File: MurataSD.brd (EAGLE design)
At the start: 50 x 52 mm, 2 parts, among them U1 IC_BLE_LBCA2HNZYZ-711, U100 BOARD_MMC

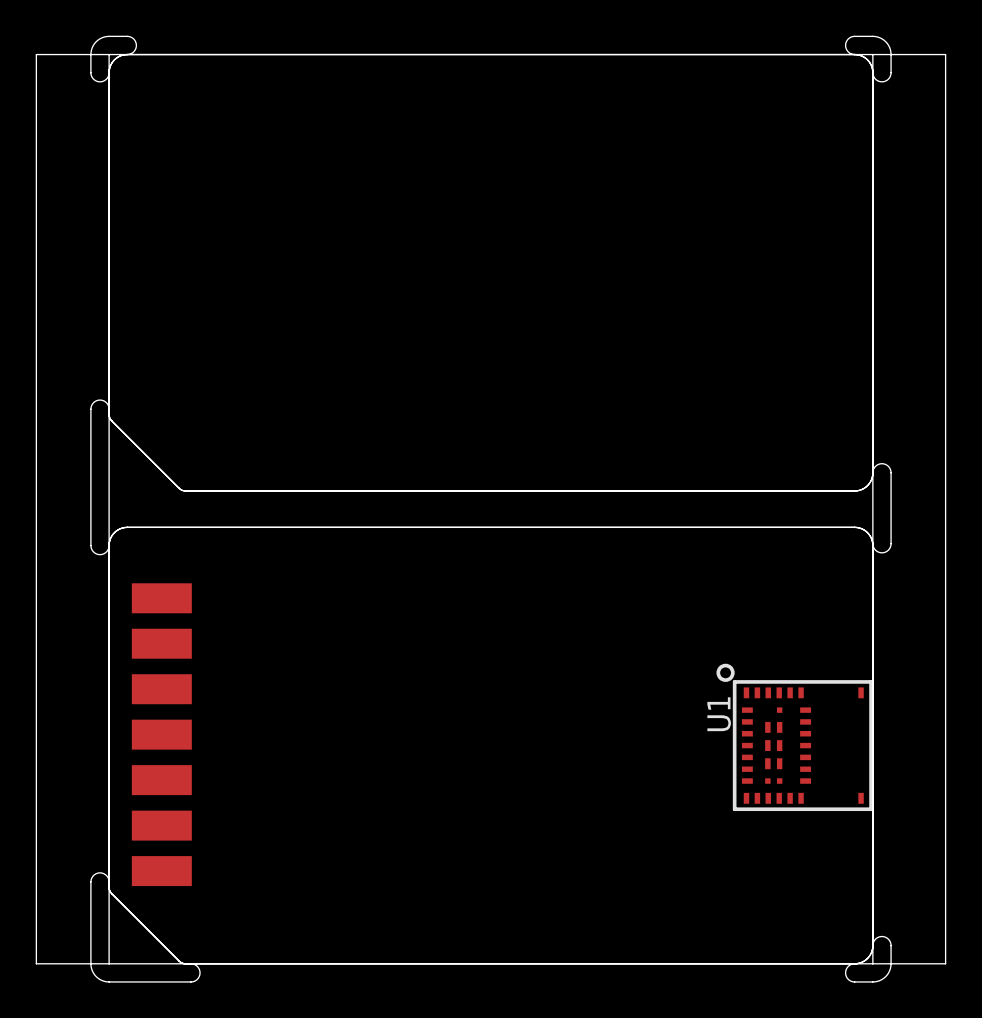
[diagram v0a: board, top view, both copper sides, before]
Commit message: schematic update
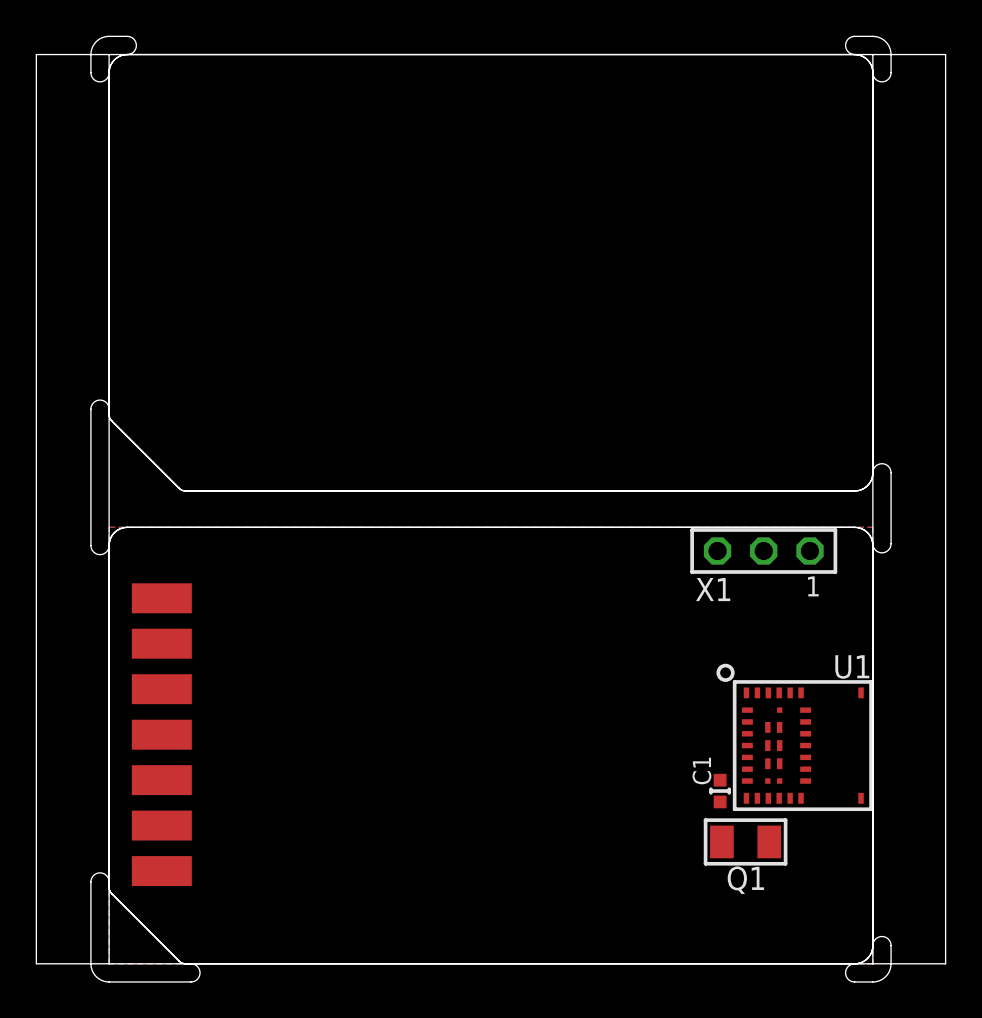
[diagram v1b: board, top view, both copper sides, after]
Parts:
- added C1: (no value), mylib:C0402
- added Q1: (no value), mylib:CR_3216
- added X1: TSW-103-02-S-S, con-samtec.local:TSW-103-02-S-S
- renumbered U100 to U2
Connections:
- new net 3.3V: C1.1, U1.7, U2.4
- new net CLK: U1.23, U2.5
- new net CS: U1.11, U2.1
- new net GND: C1.2, U1.15, U1.16, U1.17, U1.18, U1.20, U1.21, U1.26, U1.27, U1.28, U1.29, U1.32, U1.33, U1.34, U1.6, U1.8, U2.3, U2.6, X1.3
- new net MISO: U1.3, U2.7
- new net MOSI: U1.1, U2.2
- new net N$1: Q1.1, U1.9
- new net N$2: Q1.2, U1.10
- new net N$3: U1.4, X1.1
- new net N$4: U1.5, X1.2
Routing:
- added copper zone on layer 1, net GND
- added copper zone on layer 16, net GND

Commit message: [ SD ] update library
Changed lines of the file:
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@@
 <layers>
 <layer number="1" name="Top" color="4" fill="0" visible="yes" active="yes"/>
+<layer number="2" name="Route2" color="1" fill="3" visible="no" active="no"/>
+<layer number="3" name="Route3" color="4" fill="3" visible="no" active="no"/>
+<layer number="14" name="Route14" color="1" fill="6" visible="no" active="no"/>
+<layer number="15" name="Route15" color="4" fill="6" visible="no" active="no"/>
 <layer number="16" name="Bottom" color="1" fill="1" visible="yes" active="yes"/>
 <layer number="17" name="Pads" color="2" fill="1" visible="yes" active="yes"/>
 <layer number="18" name="Vias" color="2" fill="1" visible="yes" active="yes"/>
 <layer number="19" name="Unrouted" color="6" fill="1" visible="yes" active="yes"/>
-<layer number="20" name="Dimension" color="15" fill="1" visible="no" active="yes"/>
+<layer number="20" name="Dimension" color="15" fill="1" visible="yes" active="yes"/>
 <layer number="21" name="tPlace" color="7" fill="1" visible="yes" active="yes"/>
 <layer number="22" name="bPlace" color="7" fill="1" visible="yes" active="yes"/>
@@
 <layer number="45" name="Holes" color="7" fill="1" visible="no" active="yes"/>
 <layer number="46" name="Milling" color="3" fill="1" visible="no" active="yes"/>
-<layer number="47" name="Measures" color="7" fill="1" visible="no" active="yes"/>
+<layer number="47" name="Measures" color="7" fill="1" visible="yes" active="yes"/>
 <layer number="48" name="Document" color="7" fill="1" visible="yes" active="yes"/>
 <layer number="49" name="Reference" color="7" fill="1" visible="yes" active="yes"/>
@@
 <layer number="132" name="bAdjust" color="7" fill="1" visible="no" active="yes"/>
 <layer number="144" name="Drill_legend" color="7" fill="1" visible="yes" active="yes"/>
+<layer number="145" name="DrillLegend_01-16" color="2" fill="9" visible="no" active="yes"/>
+<layer number="146" name="DrillLegend_01-20" color="3" fill="9" visible="no" active="yes"/>
 <layer number="151" name="HeatSink" color="7" fill="1" visible="yes" active="yes"/>
 <layer number="152" name="_bDocu" color="7" fill="1" visible="yes" active="yes"/>
@@
 </polygon>
 <contactref element="X1" pad="3"/>
-<wire x1="39.05" y1="14.9" x2="37.46" y2="22.7" width="0" layer="19" extent="1-1"/>
-<wire x1="40.225" y1="13" x2="39.05" y2="14.9" width="0" layer="19" extent="1-1"/>
-<wire x1="40.875" y1="13" x2="40.225" y2="13" width="0" layer="19" extent="1-1"/>
-<wire x1="40.875" y1="12" x2="40.875" y2="13" width="0" layer="19" extent="1-1"/>
-<wire x1="40.225" y1="12" x2="40.875" y2="12" width="0" layer="19" extent="1-1"/>
-<wire x1="40.875" y1="11" x2="40.875" y2="12" width="0" layer="19" extent="1-1"/>
-<wire x1="40.225" y1="11" x2="40.875" y2="11" width="0" layer="19" extent="1-1"/>
-<wire x1="39.1" y1="10.7" x2="40.225" y2="11" width="0" layer="19" extent="1-1"/>
-<wire x1="42.3" y1="12" x2="40.875" y2="12" width="0" layer="19" extent="1-1"/>
-<wire x1="42.3" y1="11.35" x2="42.3" y2="12" width="0" layer="19" extent="1-1"/>
-<wire x1="42.3" y1="12.65" x2="42.3" y2="12" width="0" layer="19" extent="1-1"/>
-<wire x1="42.3" y1="10.7" x2="42.3" y2="11.35" width="0" layer="19" extent="1-1"/>
-<wire x1="42.3" y1="13.95" x2="42.3" y2="12.65" width="0" layer="19" extent="1-1"/>
-<wire x1="42.05" y1="14.9" x2="42.3" y2="13.95" width="0" layer="19" extent="1-1"/>
-<wire x1="39.05" y1="9.1" x2="39.1" y2="10.7" width="0" layer="19" extent="1-1"/>
-<wire x1="37.6" y1="8.9" x2="39.05" y2="9.1" width="0" layer="19" extent="1-1"/>
-<wire x1="6.9" y1="10.1" x2="37.6" y2="8.9" width="0" layer="19" extent="1-1"/>
-<wire x1="6.9" y1="17.6" x2="6.9" y2="10.1" width="0" layer="19" extent="1-1"/>
+<wire x1="6.9" y1="10.1" x2="6.9" y2="17.6" width="0" layer="19" extent="1-1"/>
+<wire x1="37.6" y1="8.9" x2="6.9" y2="10.1" width="0" layer="19" extent="1-1"/>
 </signal>
 <signal name="3.3V">
@@
 <contactref element="U1" pad="7"/>
 <contactref element="C1" pad="1"/>
-<wire x1="37.6" y1="10.1" x2="39.1" y2="10.05" width="0" layer="19" extent="1-1"/>
+<wire x1="37.6" y1="10.1" x2="39" y2="10.05" width="0" layer="19" extent="1-1"/>
 <wire x1="6.9" y1="12.6" x2="37.6" y2="10.1" width="0" layer="19" extent="1-1"/>
 </signal>
@@
 <contactref element="U1" pad="9"/>
 <contactref element="Q1" pad="1"/>
-<wire x1="37.7" y1="6.7" x2="39.65" y2="9.1" width="0" layer="19" extent="1-1"/>
+<wire x1="37.7" y1="6.7" x2="39.625" y2="9.1" width="0" layer="19" extent="1-1"/>
 </signal>
 <signal name="N$2">
 <contactref element="U1" pad="10"/>
 <contactref element="Q1" pad="2"/>
-<wire x1="40.3" y1="6.7" x2="40.25" y2="9.1" width="0" layer="19" extent="1-1"/>
+<wire x1="40.3" y1="6.7" x2="40.275" y2="9.1" width="0" layer="19" extent="1-1"/>
 </signal>
 <signal name="CLK">
 <contactref element="U2" pad="5"/>
 <contactref element="U1" pad="23"/>
-<wire x1="6.9" y1="15.1" x2="40.85" y2="14.9" width="0" layer="19" extent="1-1"/>
+<wire x1="6.9" y1="15.1" x2="40.925" y2="14.9" width="0" layer="19" extent="1-1"/>
 </signal>
 <signal name="MOSI">
 <contactref element="U2" pad="2"/>
 <contactref element="U1" pad="1"/>
-<wire x1="6.9" y1="7.6" x2="39.1" y2="13.95" width="0" layer="19" extent="1-1"/>
+<wire x1="6.9" y1="7.6" x2="39" y2="13.95" width="0" layer="19" extent="1-1"/>
 </signal>
 <signal name="CS">
 <contactref element="U2" pad="1"/>
 <contactref element="U1" pad="11"/>
-<wire x1="6.9" y1="5.1" x2="40.85" y2="9.1" width="0" layer="19" extent="1-1"/>
+<wire x1="6.9" y1="5.1" x2="40.925" y2="9.1" width="0" layer="19" extent="1-1"/>
 </signal>
 <signal name="MISO">
 <contactref element="U2" pad="7"/>
 <contactref element="U1" pad="3"/>
-<wire x1="6.9" y1="20.1" x2="39.1" y2="12.65" width="0" layer="19" extent="1-1"/>
+<wire x1="6.9" y1="20.1" x2="39" y2="12.65" width="0" layer="19" extent="1-1"/>
 </signal>
 <signal name="N$3">
 <contactref element="U1" pad="4"/>
 <contactref element="X1" pad="1"/>
-<wire x1="39.1" y1="12" x2="42.54" y2="22.7" width="0" layer="19" extent="1-1"/>
+<wire x1="39" y1="12" x2="42.54" y2="22.7" width="0" layer="19" extent="1-1"/>
 </signal>
 <signal name="N$4">
 <contactref element="U1" pad="5"/>
 <contactref element="X1" pad="2"/>
-<wire x1="39.1" y1="11.35" x2="40" y2="22.7" width="0" layer="19" extent="1-1"/>
+<wire x1="39" y1="11.35" x2="40" y2="22.7" width="0" layer="19" extent="1-1"/>
 </signal>
 </signals>

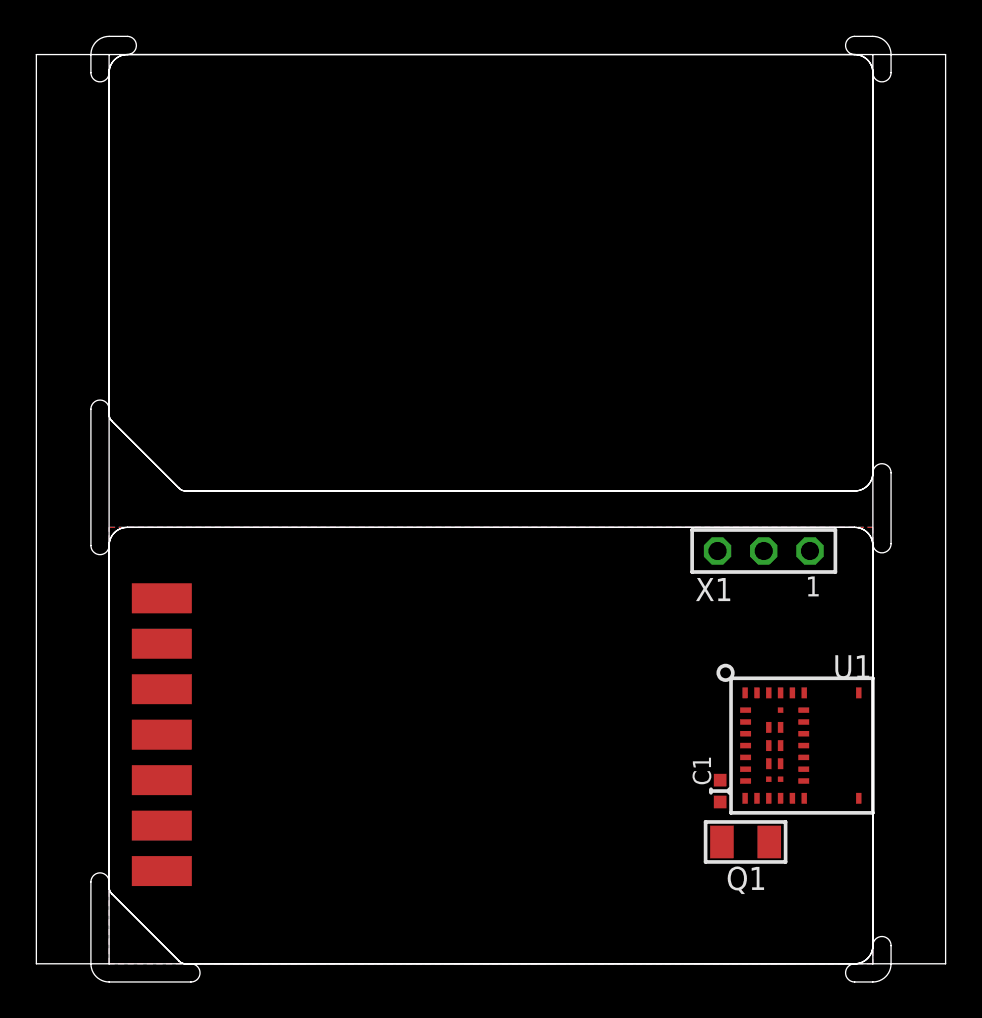
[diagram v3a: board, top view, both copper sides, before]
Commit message: [ SD ] library update; add SWD connector; add Flash;
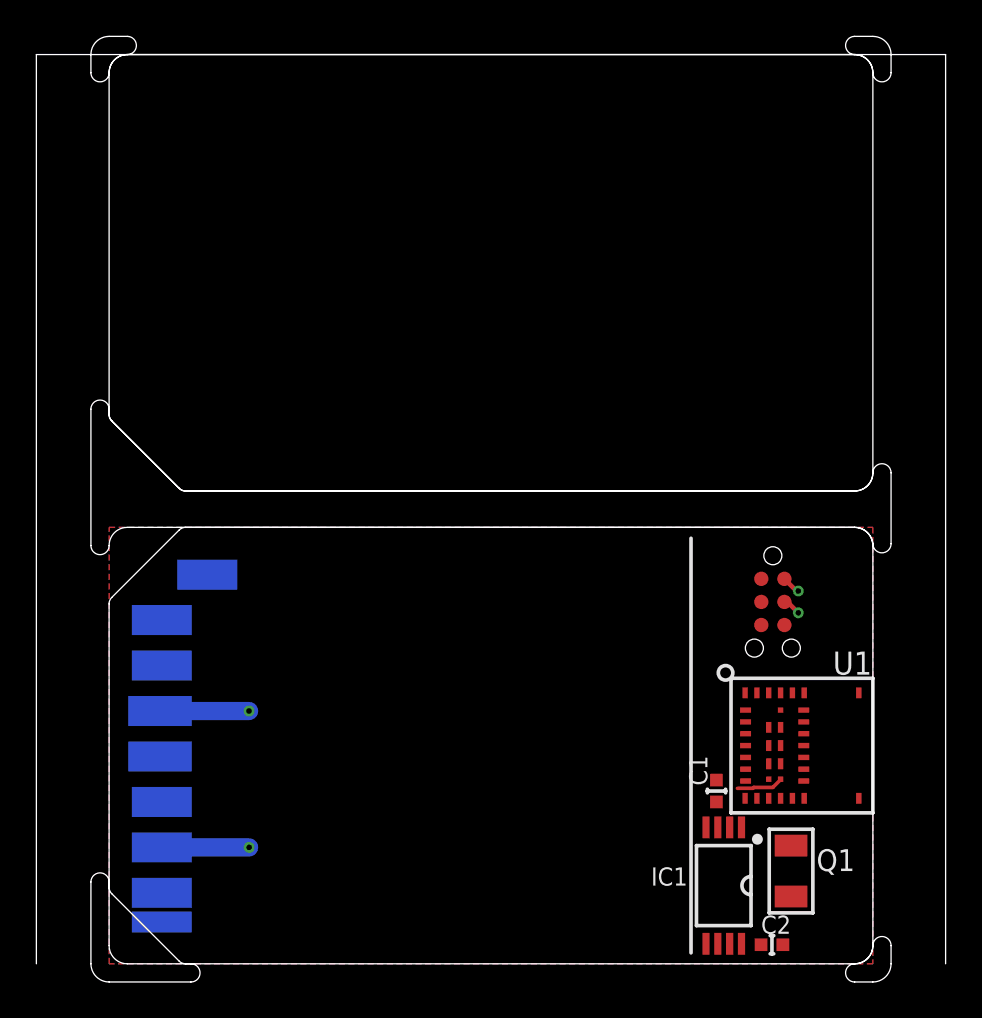
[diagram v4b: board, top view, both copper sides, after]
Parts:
- removed X1: TSW-103-02-S-S, con-samtec.local:TSW-103-02-S-S
- added C2: (no value), mylib:C0402
- added CON1: CON_TC2030-CTL-NL, mylib:CON_TC2030-IDC-NL
- added IC1: IC_MEMORY_8P_AT25XE011_TSSOP, mylib:IC_08_0.65_160MIL
- Q1: device mylib:CR_3216 -> mylib:CRYSTAL_FC-135
- U1: value IC_BLE_LBCA2HNZYZ-711 -> LBCA2HNZYZ-711
- moved Q1 2.97 mm to (41.5, 5.10), turned to 90 degrees
- moved C1 0.20 mm to (37.4, 9.50)
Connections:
- removed net N$3: U1.4, X1.1
- removed net N$4: U1.5, X1.2
- new net RESET: U1.25, U2.9
- new net SWCLK: CON1.4, U1.4
- new net SWDIO: CON1.2, U1.5
- new net VPP: U1.31, U2.8
- net 3.3V: now also C2.1, CON1.1, IC1.3, IC1.7, IC1.8
- net CLK: now also IC1.6, U1.12; no longer U1.23
- net CS: now also IC1.1
- net GND: now also C2.2, CON1.5, IC1.4; no longer X1.3
- net MISO: now also IC1.2
- net MOSI: now also IC1.5
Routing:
- net GND: track 0.00 -> 9.70 mm, vias 0 -> 2
- net VPP: track 0.00 -> 2.60 mm
- net SWDIO: track 0.00 -> 1.05 mm, vias 0 -> 1
- net SWCLK: track 0.00 -> 1.03 mm, vias 0 -> 1
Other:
- outline, holes or cut-outs redrawn

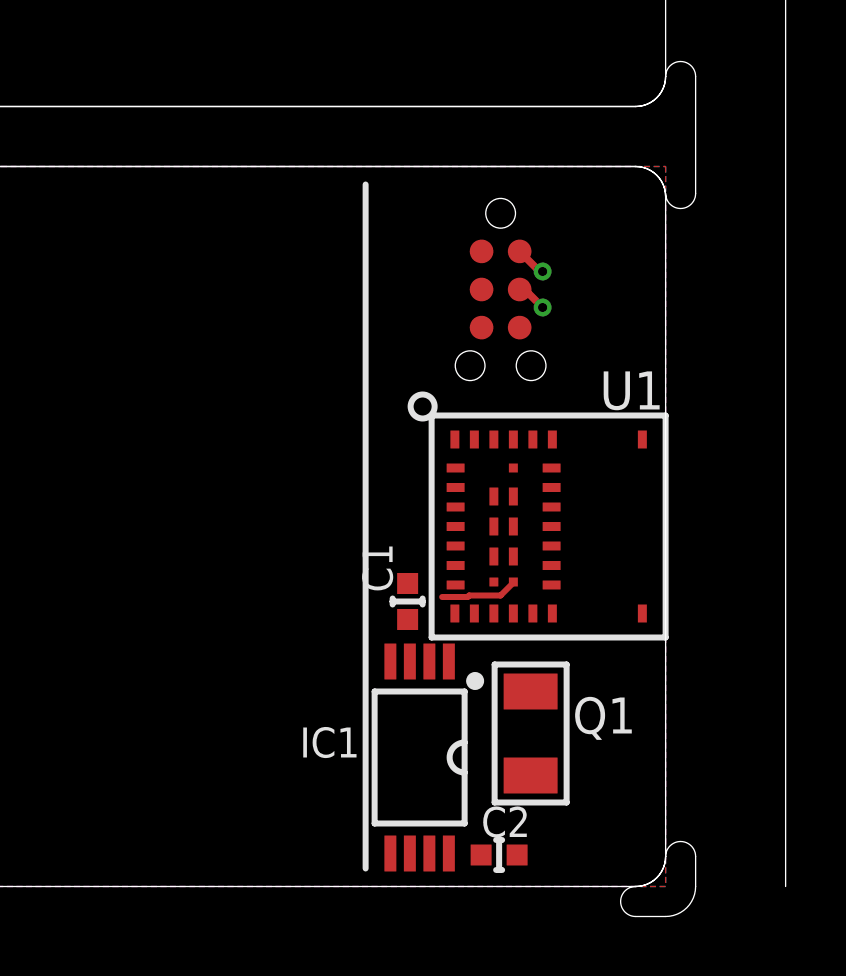
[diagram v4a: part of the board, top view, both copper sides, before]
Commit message: [ SD ] disconnect VPP; SPI uses P0_4 to P0_7
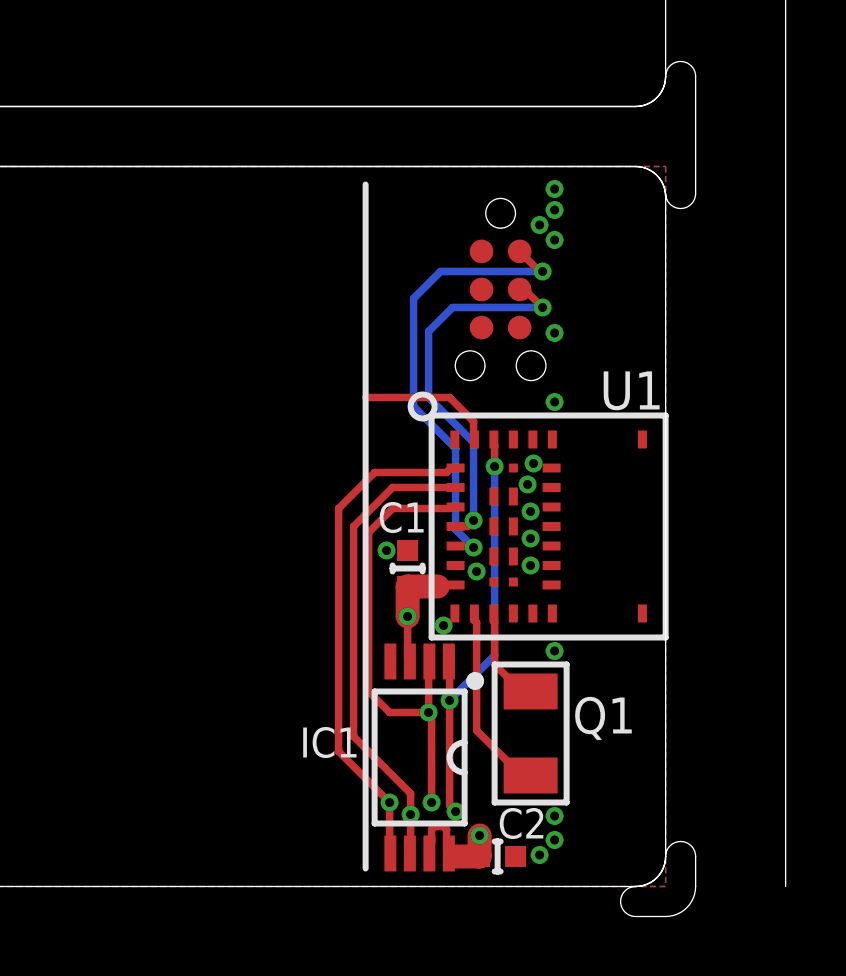
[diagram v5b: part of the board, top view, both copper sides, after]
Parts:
- moved C1 1.10 mm to (37.4, 10.6), turned to 90 degrees
- moved C2 0.07 mm to (40.4, 1.00)
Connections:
- removed net VPP: U1.31, U2.8
- new net N$4: U1.30, U2.8
- new net N$5: U1.31
- net CLK: now also U1.2; no longer U1.12
- net CS: now also U1.24; no longer U1.11
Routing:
- net MOSI: track 0.00 -> 16.7 mm, vias 0 -> 1
- net CLK: track 0.00 -> 15.6 mm, vias 0 -> 1
- net MISO: track 0.00 -> 15.6 mm, vias 0 -> 2
- net CS: track 0.00 -> 14.4 mm, vias 0 -> 3
- net SWDIO: track 1.05 -> 15.5 mm, vias 1 -> 2
- net SWCLK: track 1.03 -> 12.8 mm, vias 1 -> 2
- net 3.3V: track 0.00 -> 8.16 mm, vias 0 -> 2
- net N$1: track 0.00 -> 6.35 mm
- net RESET: track 0.00 -> 4.54 mm
- net N$2: track 0.00 -> 3.28 mm
- net VPP: track 2.60 -> 0.00 mm
- net GND: vias 2 -> 20

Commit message: [ SD ]
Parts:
- Q1: value (none) -> CRYSTAL2_32.768K_2012; device mylib:CRYSTAL_FC-135 -> mylib:CR_2125
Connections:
- net N$4: no longer U1.30
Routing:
- net 3.3V: track 8.16 -> 62.0 mm, vias 2 -> 4
- net MISO: track 15.6 -> 48.4 mm, vias 2 -> 1
- net MOSI: track 16.7 -> 47.2 mm
- net RESET: track 4.54 -> 33.3 mm, vias 0 -> 1
- net CLK: track 15.6 -> 0.00 mm, vias 1 -> 0
- net CS: track 14.4 -> 0.00 mm, vias 3 -> 0
